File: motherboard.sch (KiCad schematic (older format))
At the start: 16 parts, among them U1 STM32F411-LQFP64, U2 STM32F411-LQFP64, U3 74LVC2G132, U4 74LS125, U5 74LS125, U6 74LS125, U7 74LS125, U8 74LS125

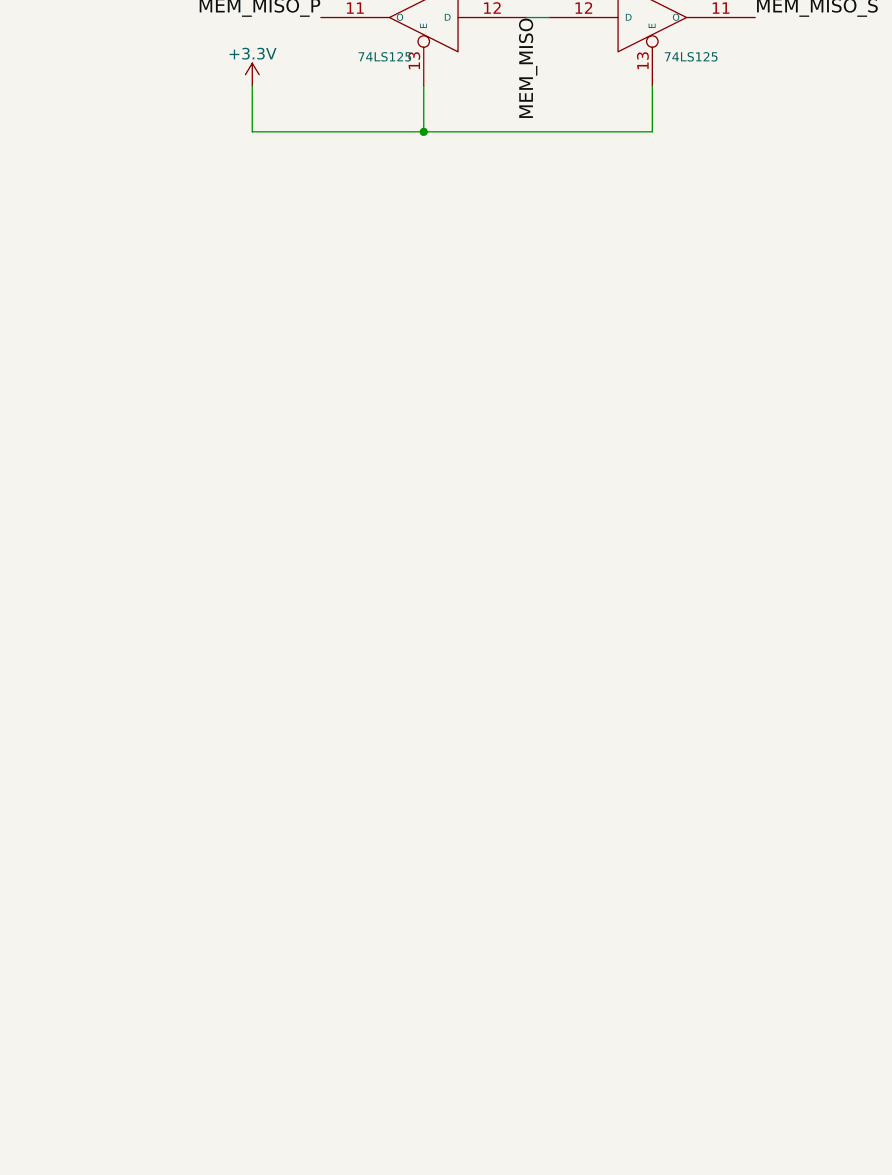
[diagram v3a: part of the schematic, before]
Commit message: Put FRAM on motherboard
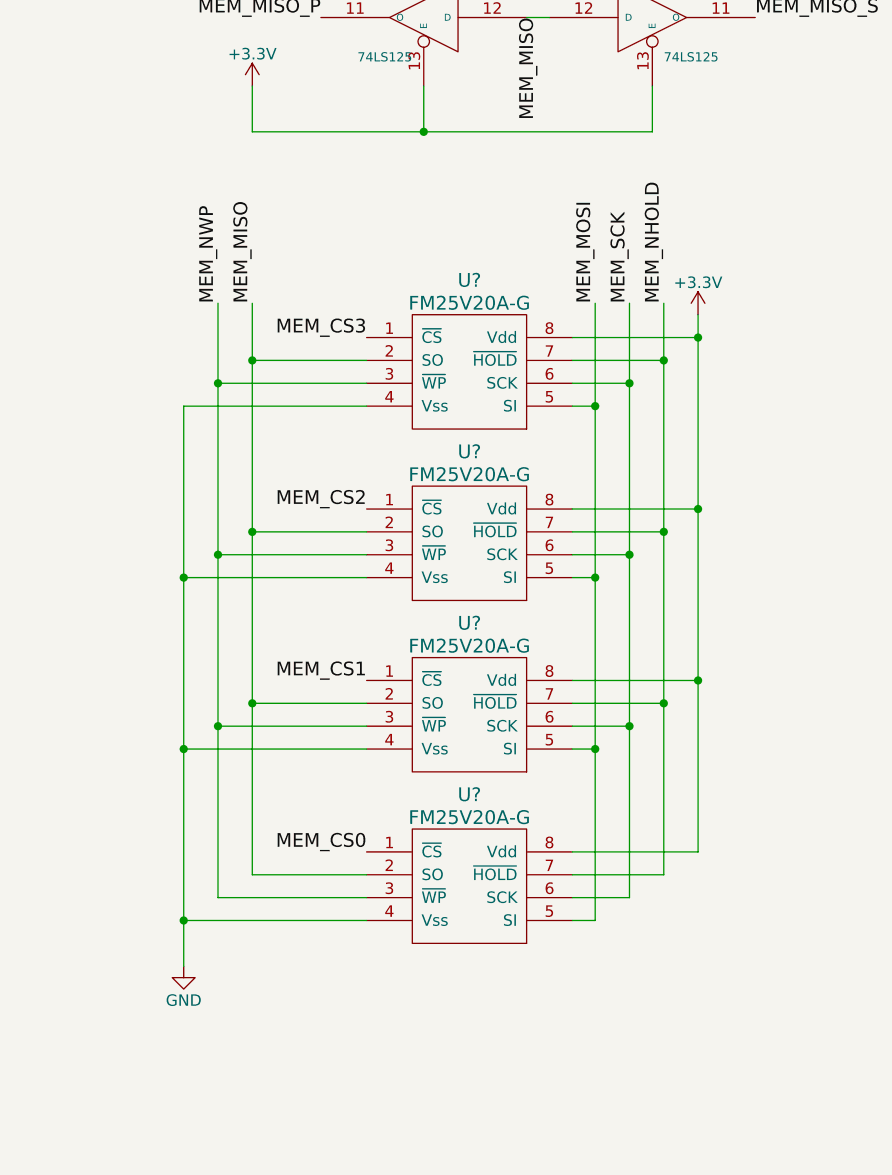
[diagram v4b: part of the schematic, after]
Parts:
- added U? (x4): FM25V20A-G, symbol FM25V20A-G
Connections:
- net +3V3: now also U?.8 (Vdd), U?.8 (Vdd), U?.8 (Vdd), U?.8 (Vdd)
- net GND: now also U?.4 (Vss), U?.4 (Vss), U?.4 (Vss), U?.4 (Vss)
- net MEM_CS0: now also U?.1 (~CS)
- net MEM_CS1: now also U?.1 (~CS)
- net MEM_CS2: now also U?.1 (~CS)
- net MEM_CS3: now also U?.1 (~CS)
- net MEM_MISO: now also U?.2 (SO), U?.2 (SO), U?.2 (SO), U?.2 (SO)
- net MEM_MOSI: now also U?.5 (SI), U?.5 (SI), U?.5 (SI), U?.5 (SI)
- net MEM_NHOLD: now also U?.7 (~HOLD), U?.7 (~HOLD), U?.7 (~HOLD), U?.7 (~HOLD)
- net MEM_NWP: now also U?.3 (~WP), U?.3 (~WP), U?.3 (~WP), U?.3 (~WP)
- net MEM_SCK: now also U?.6 (SCK), U?.6 (SCK), U?.6 (SCK), U?.6 (SCK)

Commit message: Work on schematic
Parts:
- removed R3, R4: 100K, symbol R
- added C? (x4): 1uF, symbol C
- added C? (x12): 0.1uF, symbol C
- added C? (x4): 4.3pF, symbol C
- added C? (x4): 20pF, symbol C
- added C? (x2): 4.7uF, symbol C
- added L? (x2): BEAD, symbol INDUCTOR_SMALL
- added R? (x12): 100K, symbol R
- added unit 4 of U1
- added unit 4 of U2
- added U9: APE8865N-33-HF-3, SOT-23, symbol APE8865N-33-HF-3
- added Y? (x2): 32k, symbol Crystal
- added Y? (x2): 8M(16pF), symbol Crystal
- gave numbers to parts that had none: 5
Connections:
- net +3V3: now also C?.1, C?.2, C?.2, C?.2, C?.2, C?.2, C?.2, C?.2, C?.2, C?.2, L?.2, R?.1, R?.1, R?.1, R?.1, R?.2, R?.2, R?.2, R?.2, R?.2, R?.2, U1.1 (VBAT), U1.19 (VDD), U1.32 (VDD), U1.48 (VDD), U1.64 (VDD), U9.3 (VIN); no longer U4.13 (E), U5.13 (E), U6.1 (E), U6.4 (E)
- net GND: now also C?.1, C?.1, C?.1, C?.1, C?.1, C?.1, C?.1, C?.1, C?.1, C?.1, C?.1, C?.1, C?.1, C?.1, C?.1, C?.1, C?.1, C?.1, C?.1, C?.1, C?.1, C?.1, C?.1, C?.1, C?.2, C?.2, R?.1, R?.1, U1.12 (VSSA/VREF-), U1.18 (VSS), U1.31 (VSS), U1.43 (VSS), U1.47 (VSS), U2.12 (VSSA/VREF-), U2.18 (VSS), U2.31 (VSS), U2.43 (VSS), U2.47 (VSS), U9.1 (GND)
- net MEM_CS2_P: now also U1.27 (PB1); no longer U1.28 (PB2)
- net MEM_CS2_S: now also U2.27 (PB1); no longer U2.28 (PB2)
- net MEM_CS3_P: now also U1.26 (PB0); no longer U1.27 (PB1)
- net MEM_CS3_S: now also U2.26 (PB0); no longer U2.27 (PB1)
- net MEM_NHOLD: now also U14.8 (O); no longer U14.3 (O)
- net MEM_NHOLD_S: now also U14.9 (D); no longer U14.2 (D)
- net MEM_NWP: now also U14.11 (O), U14.6 (O); no longer U14.3 (O), U14.3 (O)
- net MEM_NWP_P: now also U14.5 (D); no longer U14.2 (D)
- net MEM_NWP_S: now also U14.12 (D); no longer U14.2 (D)
- net NBUFEN_PRI: now also U14.4 (E); no longer U14.1 (E)
- net NBUFEN_SEC: now also U14.10 (E), U14.13 (E); no longer U14.1 (E), U14.1 (E)
- net PRX_STX: now also R?.1
- net PTX_SRX: now also R?.1
- net NRST_PRI renamed NRST_P
- net NRST_P: now also R?.1, U1.7 (NRST)
- net NRST_SEC renamed NRST_S
- net NRST_S: now also R?.1, U2.7 (NRST)
- new net: U4.13 (E), U5.13 (E)
- new net: U6.1 (E), U6.4 (E)
- new net: L?.1, U1.13 (VDDA/VREF+)
- new net: C?.2, U1.3 (PC14-OSC32_IN), Y?.1
- new net: C?.2, U1.30 (VCAP1)
- new net: C?.2, U1.4 (PC15-OSC32_OUT), Y?.2
- new net: C?.2, U1.5 (PH0-OSC_IN), Y?.1
- new net: C?.2, U1.6 (PH1-OSC_OUT), Y?.2
- new net: L?.1, U2.13 (VDDA/VREF+)
- new net: C?.2, U2.3 (PC14-OSC32_IN), Y?.1
- new net: C?.2, U2.30 (VCAP1)
- new net: C?.2, U2.4 (PC15-OSC32_OUT), Y?.2
- new net: C?.2, U2.5 (PH0-OSC_IN), Y?.1
- new net: C?.2, U2.6 (PH1-OSC_OUT), Y?.2
- new net BOOT0_P: R?.2, U1.60 (BOOT0)
- new net BOOT0_S: R?.2, U2.60 (BOOT0)
- new net BOOT1_P: R?.1, U1.28 (PB2)
- new net BOOT1_S: R?.1, U2.28 (PB2)
- new net VDD_S: C?.1, C?.2, C?.2, C?.2, C?.2, C?.2, L?.2, U2.1 (VBAT), U2.19 (VDD), U2.32 (VDD), U2.48 (VDD), U2.64 (VDD), U9.2 (VOUT)
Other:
- moved on the sheet: U3A, U3B

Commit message: Very nearly done
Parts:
- removed unit 2 of U3
- removed U4, U5, U6, U7, U8: 74LS125, symbol 74LS125
- removed U9: APE8865N-33-HF-3, SOT-23, symbol APE8865N-33-HF-3
- added P? (x2): CONN_01X08, symbol CONN_01X08
- added R16, R9: 100K, symbol R
- added R17, R18, R19, R20, R21, R22: 4.7K, symbol R
- added TP1, TP10, TP11, TP12, TP13, TP2, TP3, TP4, TP5, TP6, TP7, TP8, TP9, TP?: TP, symbol TP
- added U10, U11, U12, U13, U9: 74LS125, symbol 74LS125
- added U15, U16: PCA9517A, symbol PCA9517A
- added U3: AP7313, SOT-23, symbol AP7313
- added unit 2 of U4
- gave numbers to parts that had none: 44
- renumbered R5 to R14, R6 to R15, U3 to U4, U10 to U5, U11 to U6, U12 to U7, U13 to U8
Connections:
- net NSS_PRI is gone; now on net NRST_P: U4.1
- net +3V3: now also R14.2, R17.1, R18.1, R19.1, R20.1, R21.1, R22.1, U10.14 (VCC), U10.14 (VCC), U10.14 (VCC), U10.14 (VCC), U11.14 (VCC), U11.14 (VCC), U11.14 (VCC), U11.14 (VCC), U12.14 (VCC), U12.14 (VCC), U12.14 (VCC), U12.14 (VCC), U13.14 (VCC), U13.14 (VCC), U13.14 (VCC), U13.14 (VCC), U15.1 (VCCA), U15.8 (VCCB), U16.1 (VCCA), U16.8 (VCCB), U3.1 (VIN), U4.8 (VCC), U9.14 (VCC), U9.14 (VCC), U9.14 (VCC), U9.14 (VCC); no longer R14.1
- net GND: now also P?.1 (P1), P?.1 (P1), P?.8 (P8), P?.8 (P8), R9.2, U10.7 (GND), U10.7 (GND), U10.7 (GND), U10.7 (GND), U11.7 (GND), U11.7 (GND), U11.7 (GND), U11.7 (GND), U12.7 (GND), U12.7 (GND), U12.7 (GND), U12.7 (GND), U13.7 (GND), U13.7 (GND), U13.7 (GND), U13.7 (GND), U15.4 (GND), U16.4 (GND), U3.3 (GND), U4.4 (GND), U9.7 (GND), U9.7 (GND), U9.7 (GND), U9.7 (GND)
- net MEM_CS0: now also R13.2, TP6.1, U12.6 (O), U12.8 (O)
- net MEM_CS0_P: now also U12.5 (D)
- net MEM_CS0_S: now also U12.9 (D)
- net MEM_CS1: now also R12.2, TP7.1, U12.11 (O), U12.3 (O)
- net MEM_CS1_P: now also U12.2 (D)
- net MEM_CS1_S: now also U12.12 (D)
- net MEM_CS2: now also R11.2, TP8.1, U11.6 (O), U11.8 (O)
- net MEM_CS2_P: now also U11.5 (D)
- net MEM_CS2_S: now also U11.9 (D)
- net MEM_CS3: now also R10.2, TP9.1, U11.11 (O), U11.3 (O)
- net MEM_CS3_P: now also U11.2 (D)
- net MEM_CS3_S: now also U11.12 (D)
- net MEM_MISO: now also TP11.1, U9.12 (D), U9.2 (D), U9.5 (D), U9.9 (D)
- net MEM_MISO_P: now also U9.6 (O)
- net MEM_MISO_S: now also U9.11 (O)
- net MEM_MOSI: now also TP10.1, U13.6 (O), U13.8 (O)
- net MEM_MOSI_P: now also U13.5 (D)
- net MEM_MOSI_S: now also U13.9 (D)
- net MEM_NHOLD: now also TP5.1, U10.11 (O), U10.3 (O); no longer U14.3 (O), U14.8 (O)
- net MEM_NHOLD_P: now also U10.2 (D); no longer U14.2 (D)
- net MEM_NHOLD_S: now also U10.12 (D); no longer U14.9 (D)
- net MEM_NWP: now also TP4.1, U10.6 (O), U10.8 (O); no longer U14.11 (O), U14.6 (O)
- net MEM_NWP_P: now also U10.5 (D); no longer U14.5 (D)
- net MEM_NWP_S: now also U10.9 (D); no longer U14.12 (D)
- net MEM_SCK: now also U13.11 (O), U13.3 (O)
- net MEM_SCK_P: now also U13.2 (D)
- net MEM_SCK_S: now also U13.12 (D)
- net NBUFEN_PRI: now also R14.1, R16.1, TP13.1, U10.1 (E), U10.4 (E), U11.1 (E), U11.4 (E), U12.1 (E), U12.4 (E), U13.1 (E), U13.4 (E), U16.5 (EN), U4.5, U4.6; no longer R14.2
- net NBUFEN_SEC: now also TP12.1, U10.10 (E), U10.13 (E), U11.10 (E), U11.13 (E), U12.10 (E), U12.13 (E), U13.10 (E), U13.13 (E), U15.5 (EN), U4.7
- net NRST_P: now also U2.50 (PA15), P?.7 (P7), TP2.1; no longer U2.2 (PC13), U4.2
- net NRST_S: now also U1.50 (PA15), P?.7 (P7), TP1.1; no longer U1.2 (PC13)
- net RADIO_RX_R: now also U9.3 (O)
- net RADIO_RX_S: now also U9.8 (O)
- net RADIO_TX: now also U14.11 (O), U14.3 (O)
- net RADIO_TX_P: now also U14.2 (D)
- net RADIO_TX_S: now also U14.12 (D)
- net SYS_SCL: now also R21.2, U15.7 (SCLB), U16.7 (SCLB)
- net SYS_SCL_P: now also R17.2, U15.2 (SCLA)
- net SYS_SCL_S: now also R19.2, U16.2 (SCLA)
- net SYS_SDA_P: now also R18.2, U15.3 (SDAA)
- net SYS_SDA_S: now also R20.2, U16.3 (SDAA)
- net UART2_RX: now also P?.6 (P6)
- net UART2_TX: now also P?.5 (P5)
- net UART3_RX: now also P?.6 (P6)
- net UART3_TX: now also P?.5 (P5)
- net VDD_S: now also TP?.1, U3.2 (VOUT)
- net NYIELD_P: now reaches U1.41 (PA8)
- net NYIELD_P: now also U4.2, R9.1, TP3.1
- net TMS_P: now reaches U1.46 (PA13)
- net TMS_P: now also P?.2 (P2)
- net TCK_P: now reaches U1.49 (PA14)
- net TCK_P: now also P?.3 (P3)
- net SWO_P: now reaches U1.55 (PB3)
- net SWO_P: now also P?.4 (P4)
- net TMS_S: now reaches U2.46 (PA13)
- net TMS_S: now also P?.2 (P2)
- net TCK_S: now reaches U2.49 (PA14)
- net TCK_S: now also P?.3 (P3)
- net SWO_S: now reaches U2.55 (PB3)
- net SWO_S: now also P?.4 (P4)
- new net: U9.1 (E), U9.10 (E)
- new net: U9.13 (E), U9.4 (E)
- new net SYS_RESET: U14.6 (O), U14.8 (O)
- new net SYS_RESET_P: U14.5 (D)
- new net SYS_RESET_S: U14.9 (D)
- new net SYS_SDA: R22.2, U15.6 (SDAB), U16.6 (SDAB)
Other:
- moved on the sheet: C23, C24, C25, C26, R1, R10, R11, R12, R13, R14, R15, R2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

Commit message: Shit's done, yo
The schematic, that is.
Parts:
- added P3: CONN_01X29, symbol CONN_01X29
- added P4: CONN_01X25, symbol CONN_01X25
- added R23, R24: 100K, symbol R
- gave numbers to parts that had none: 3
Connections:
- net RADIO_RX_R is gone; now on net RADIO_RX_P: U9.3 (O)
- net +3V3: now also P3.2 (P2), R23.1, R24.2; no longer C11.1, U3.1 (VIN)
- net GND: now also R16.2, U9.1 (E), U9.10 (E), U9.13 (E), U9.4 (E), P3.1 (P1), P4.1 (P1)
- net MEM_CS1_P: now also U1.61 (PB8); no longer U1.29 (PB10)
- net MEM_CS1_S: now also U2.61 (PB8); no longer U2.29 (PB10)
- net MEM_MISO: no longer U9.2 (D), U9.9 (D)
- net MEM_NHOLD: now also R24.1
- net MEM_NHOLD_P: now also U1.57 (PB5)
- net MEM_NHOLD_S: now also U2.57 (PB5)
- net MEM_NWP: now also R23.2
- net MEM_NWP_P: now also U1.56 (PB4)
- net MEM_NWP_S: now also U2.56 (PB4)
- net RADIO_TX: now also P3.5 (P5)
- net SPI2_MISO: now also P4.5 (P5)
- net SPI2_MOSI: now also P4.6 (P6)
- net SPI2_NSS: now also P4.3 (P3)
- net SPI2_SCK: now also P4.4 (P4)
- net SYS_RESET: now also P3.7 (P7)
- net SYS_RESET_P: now also U1.44 (PA11)
- net SYS_RESET_S: now also U2.44 (PA11)
- net SYS_SCL: now also P3.3 (P3)
- net SYS_SDA: now also P3.4 (P4)
- net SYS_SPI_MISO: now also P3.10 (P10)
- net SYS_SPI_MOSI: now also P3.11 (P11)
- net SYS_SPI_NSS: now also P3.8 (P8)
- net SYS_SPI_SCK: now also P3.9 (P9)
- net GPIO0: now reaches U1.14 (PA0)
- net GPIO0: now also P3.14 (P14)
- net GPIO1: now reaches U1.15 (PA1)
- net GPIO1: now also P3.15 (P15)
- net GPIO2: now reaches U1.45 (PA12)
- net GPIO2: now also P3.16 (P16)
- net I2C2_SDA: now reaches U1.62 (PB9)
- net I2C2_SDA: now also P3.13 (P13)
- net GPIO5: now reaches U1.10 (PC2)
- net GPIO5: now also P3.19 (P19)
- net GPIO6: now reaches U1.11 (PC3)
- net GPIO6: now also P3.20 (P20)
- net GPIO14: now reaches U1.2 (PC13)
- net GPIO14: now also P3.28 (P28)
- net GPIO7: now reaches U1.24 (PC4)
- net GPIO7: now also P3.21 (P21)
- net GPIO8: now reaches U1.25 (PC5)
- net GPIO8: now also P3.22 (P22)
- net GPIO9: now reaches U1.39 (PC8)
- net GPIO9: now also P3.23 (P23)
- net GPIO10: now reaches U1.40 (PC9)
- net GPIO10: now also P3.24 (P24)
- net GPIO11: now reaches U1.51 (PC10)
- net GPIO11: now also P3.25 (P25)
- net GPIO12: now reaches U1.52 (PC11)
- net GPIO12: now also P3.26 (P26)
- net GPIO13: now reaches U1.53 (PC12)
- net GPIO13: now also P3.27 (P27)
- net GPIO3: now reaches U1.8 (PC0)
- net GPIO3: now also P3.17 (P17)
- net GPIO4: now reaches U1.9 (PC1)
- net GPIO4: now also P3.18 (P18)
- net SGPIO0: now reaches U2.14 (PA0)
- net SGPIO0: now also P4.9 (P9)
- net SGPIO1: now reaches U2.15 (PA1)
- net SGPIO1: now also P4.10 (P10)
- net SGPIO2: now reaches U2.41 (PA8)
- net SGPIO2: now also P4.11 (P11)
- net SGPIO3: now reaches U2.45 (PA12)
- net SGPIO3: now also P4.12 (P12)
- net I2C3_SDA: now reaches U2.62 (PB9)
- net I2C3_SDA: now also P4.8 (P8)
- net SGPIO6: now reaches U2.10 (PC2)
- net SGPIO6: now also P4.15 (P15)
- net SGPIO7: now reaches U2.11 (PC3)
- net SGPIO7: now also P4.16 (P16)
- net SGPIO15: now reaches U2.2 (PC13)
- net SGPIO15: now also P4.24 (P24)
- net SGPIO8: now reaches U2.24 (PC4)
- net SGPIO8: now also P4.17 (P17)
- net SGPIO9: now reaches U2.25 (PC5)
- net SGPIO9: now also P4.18 (P18)
- net SGPIO10: now reaches U2.39 (PC8)
- net SGPIO10: now also P4.19 (P19)
- net SGPIO11: now reaches U2.40 (PC9)
- net SGPIO11: now also P4.20 (P20)
- net SGPIO12: now reaches U2.51 (PC10)
- net SGPIO12: now also P4.21 (P21)
- net SGPIO13: now reaches U2.52 (PC11)
- net SGPIO13: now also P4.22 (P22)
- net SGPIO14: now reaches U2.53 (PC12)
- net SGPIO14: now also P4.23 (P23)
- net SGPIO4: now reaches U2.8 (PC0)
- net SGPIO4: now also P4.13 (P13)
- net SGPIO5: now reaches U2.9 (PC1)
- net SGPIO5: now also P4.14 (P14)
- net GPIO15: now reaches U1.54 (PD2)
- net GPIO15: now also P3.29 (P29)
- net SGPIO16: now reaches U2.54 (PD2)
- net SGPIO16: now also P4.25 (P25)
- new net +5V: C11.1, P4.2 (P2), U3.1 (VIN)
- new net I2C2_SCL: P3.12 (P12), U1.29 (PB10)
- new net I2C3_SCL: P4.7 (P7), U2.29 (PB10)
- new net RADIO_RX: P3.6 (P6), U9.2 (D), U9.9 (D)
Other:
- note added: "SECONDARY ONLY"
- note added: "SHARED/PRIMARY"
- moved on the sheet: C15, C3, P1, P2, R1, R2, R3, R4, R5, R6, R7, R8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
